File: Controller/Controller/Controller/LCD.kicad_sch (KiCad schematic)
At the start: 46 parts, among them IC1 LTC1261L, J8 Conn_01x06_MountingPin, J9 Conn_01x50_MountingPin, Q1 CSD16323Q3, U4 LM317L_SO8, U5 AMS1117-3.3, U6 LM317L_SO8, U7 LM3488, U8 C85037, U9 LM317L_SO8

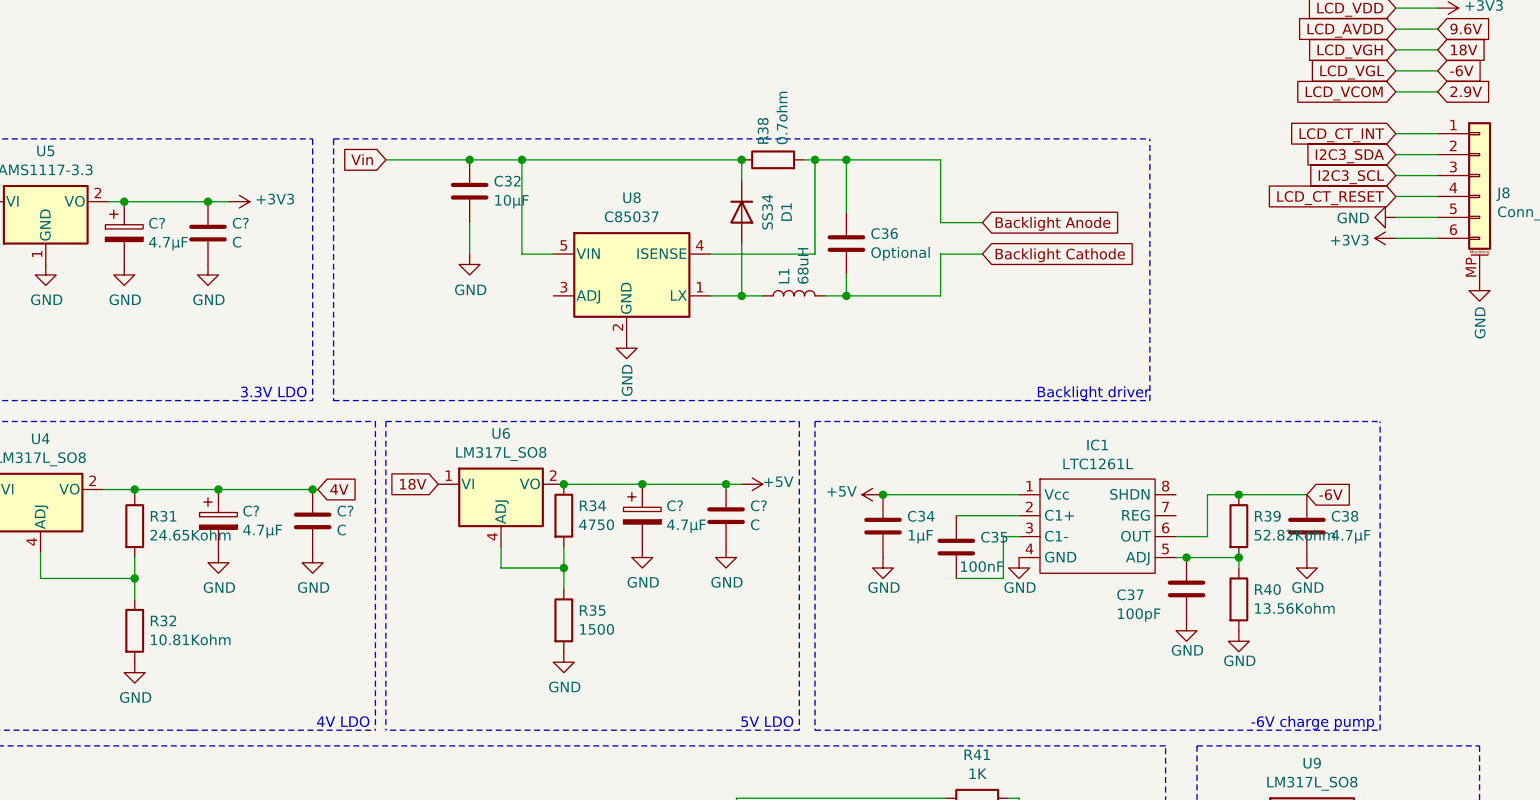
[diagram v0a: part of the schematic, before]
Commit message: changed LCDboard to Controller
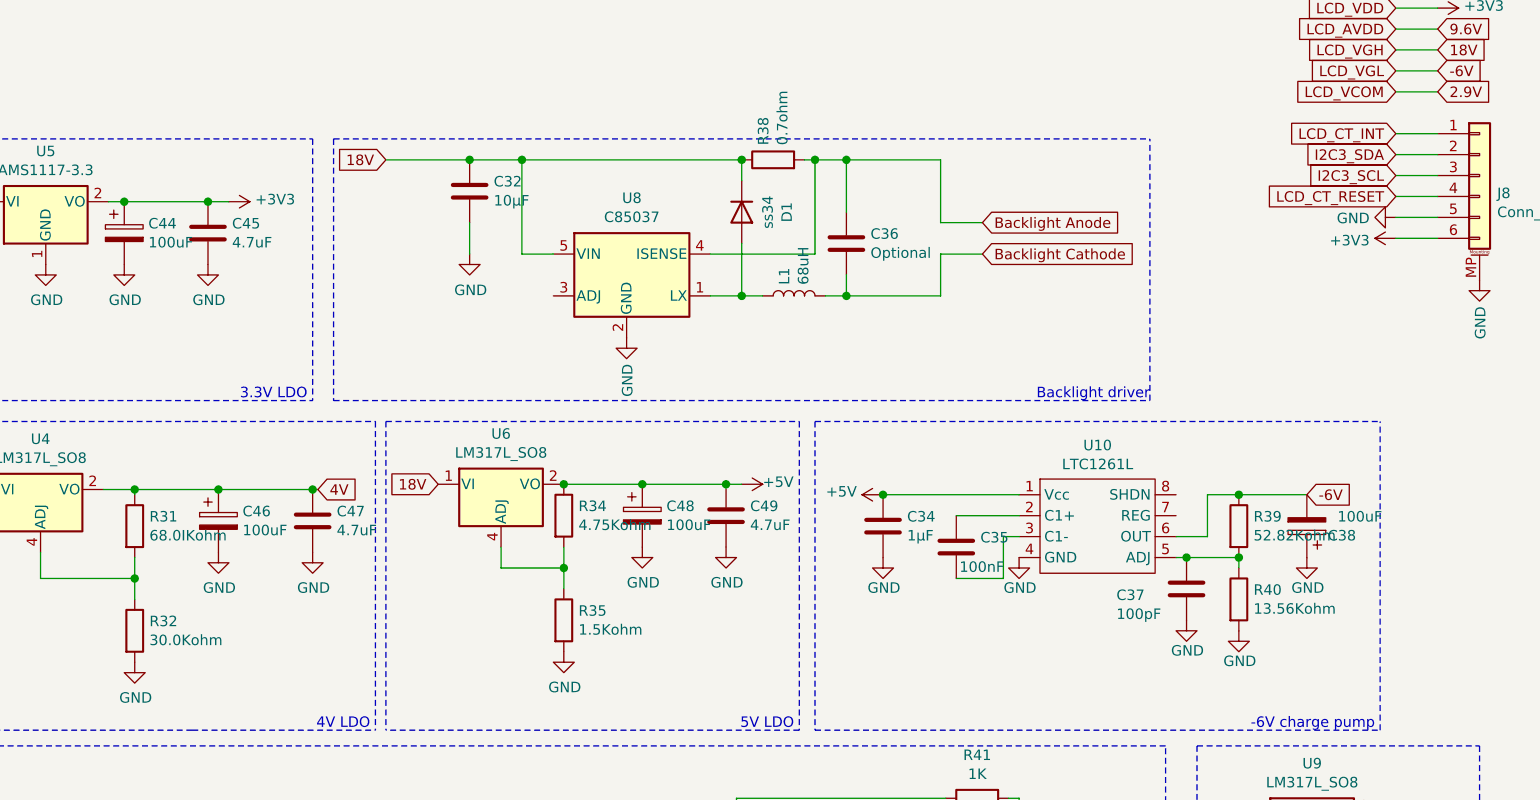
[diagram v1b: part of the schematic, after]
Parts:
- removed C38: 4.7µF, symbol Device:C
- added C38: 100uF, Capacitor_SMD:CP_Elec_5x5.4, symbol Device:CP
- C28: footprint (none) -> Capacitor_SMD:CP_Elec_8x10; LCSC (none) -> C249647
- C29, C35: footprint (none) -> Capacitor_SMD:C_0805_2012Metric_Pad1.18x1.45mm_HandSolder
- C30: footprint (none) -> Capacitor_SMD:C_0805_2012Metric_Pad1.18x1.45mm_HandSolder; LCSC (none) -> C1829
- C31: footprint (none) -> Capacitor_SMD:C_0805_2012Metric_Pad1.18x1.45mm_HandSolder; LCSC (none) -> C282778
- C32: footprint Capacitor_SMD:C_1206_3216Metric_Pad1.42x1.75mm_HandSolder -> Capacitor_SMD:C_0805_2012Metric_Pad1.18x1.45mm_HandSolder; LCSC (none) -> C17024
- C33: footprint (none) -> Capacitor_SMD:C_0805_2012Metric_Pad1.18x1.45mm_HandSolder; LCSC (none) -> C157608
- C34: footprint (none) -> Capacitor_SMD:C_0805_2012Metric_Pad1.18x1.45mm_HandSolder; LCSC (none) -> C50683
- C36: footprint Capacitor_SMD:C_0805_2012Metric_Pad1.15x1.40mm_HandSolder -> Capacitor_SMD:C_1206_3216Metric_Pad1.33x1.80mm_HandSolder
- C37: footprint (none) -> Capacitor_SMD:C_0805_2012Metric_Pad1.18x1.45mm_HandSolder; LCSC (none) -> C82028
- C39: footprint (none) -> Capacitor_SMD:CP_Elec_10x12.6; LCSC (none) -> C250070
- C44, C46, C48: renamed from C?; value 4.7µF -> 100uF; footprint (none) -> Capacitor_SMD:CP_Elec_5x5.4
- C45, C47, C49: renamed from C?; value C -> 4.7uF; footprint (none) -> Capacitor_SMD:C_0805_2012Metric_Pad1.18x1.45mm_HandSolder; LCSC (none) -> C415307
- D1: value SS34 -> ss34; LCSC (none) -> C83961
- D2: footprint (none) -> Diode_SMD:D_SMA_Handsoldering; LCSC (none) -> C83961
- J8: footprint (none) -> Connector_FFC-FPC:Hirose_FH12-6S-0.5SH_1x06-1MP_P0.50mm_Horizontal; LCSC (none) -> C528032
- J9: footprint (none) -> 00_Custom_Kicad:FPC_50; LCSC (none) -> C11098
- L2: footprint (none) -> Inductor_SMD:L_6.3x6.3_H3; LCSC (none) -> C326333
- R31: value 24.65Kohm -> 68.0IKohm; footprint (none) -> Resistor_SMD:R_0805_2012Metric_Pad1.20x1.40mm_HandSolder; LCSC (none) -> C294735
- R32: value 10.81Kohm -> 30.0Kohm; footprint (none) -> Resistor_SMD:R_0805_2012Metric_Pad1.20x1.40mm_HandSolder; LCSC (none) -> C40087
- R34: value 4750 -> 4.75Kohm; footprint (none) -> Resistor_SMD:R_0805_2012Metric_Pad1.20x1.40mm_HandSolder; LCSC (none) -> C706245
- R35: value 1500 -> 1.5Kohm; footprint (none) -> Resistor_SMD:R_0805_2012Metric_Pad1.20x1.40mm_HandSolder; LCSC (none) -> C203762
- R36: footprint (none) -> Resistor_SMD:R_0805_2012Metric_Pad1.20x1.40mm_HandSolder
- U10: renamed from IC1; footprint (none) -> Package_SO:MSOP-8_3x3mm_P0.65mm
- U7: footprint (none) -> Package_SO:MSOP-8_3x3mm_P0.65mm; LCSC (none) -> C80773
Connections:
- net -6V: now also C38.2
- net 18V: now also C32.1, D1.1 (K), R38.1, U8.5 (VIN)
- net GND: now also C38.1
- net Vin: no longer C32.1, D1.1 (K), R38.1, U8.5 (VIN)

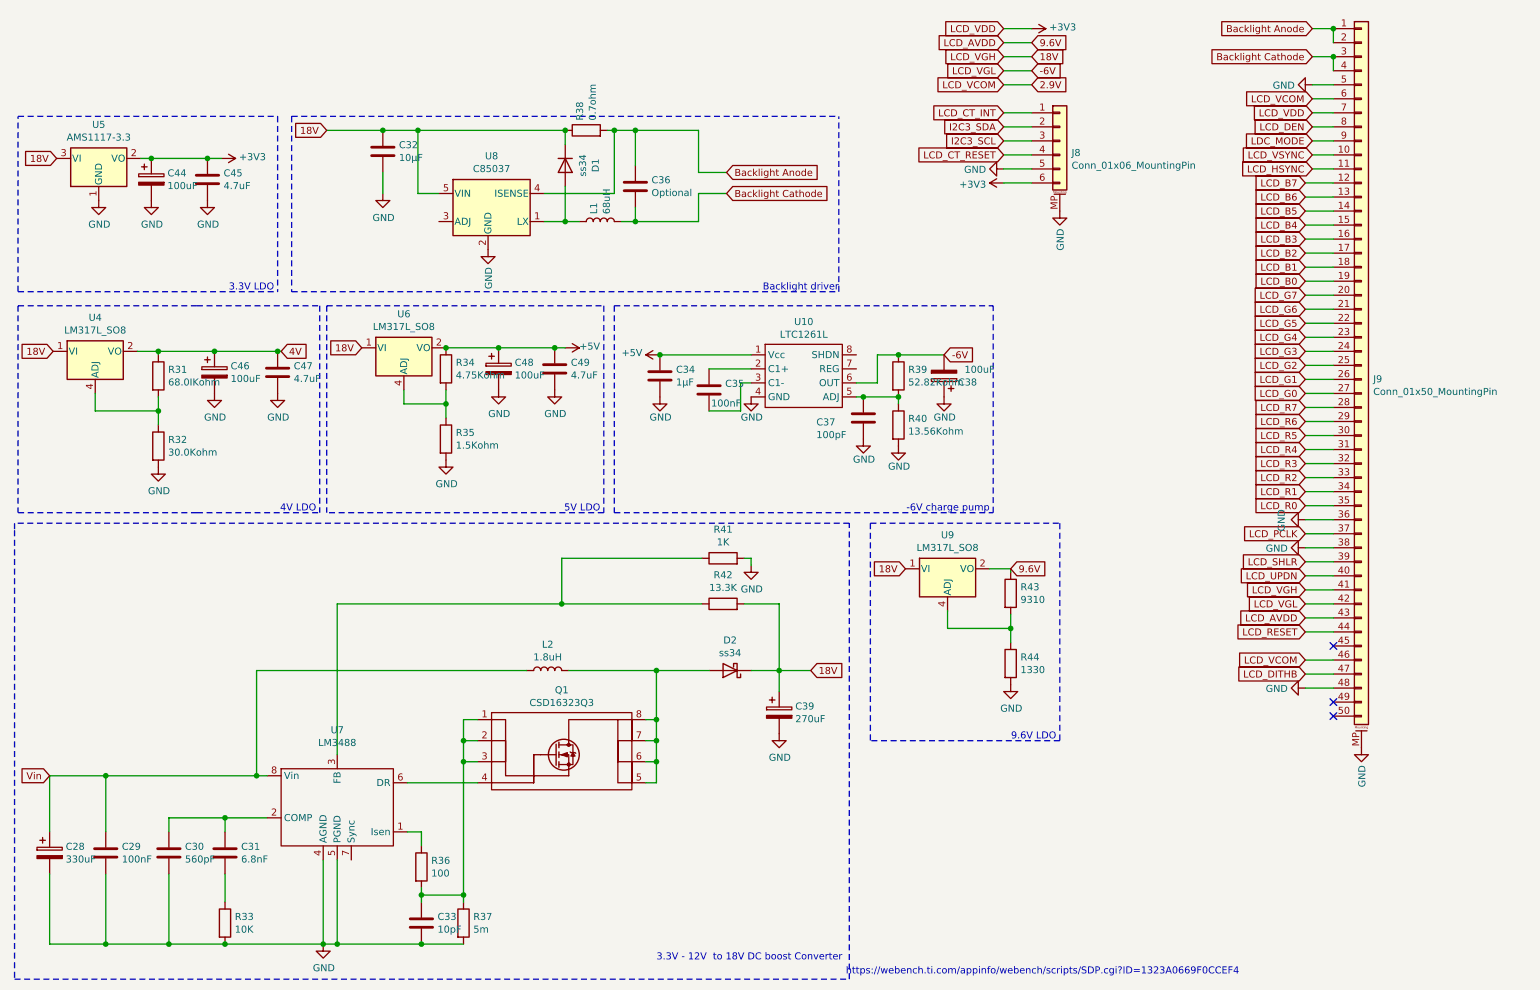
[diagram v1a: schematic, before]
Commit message: Rev 1 LCD contoller board
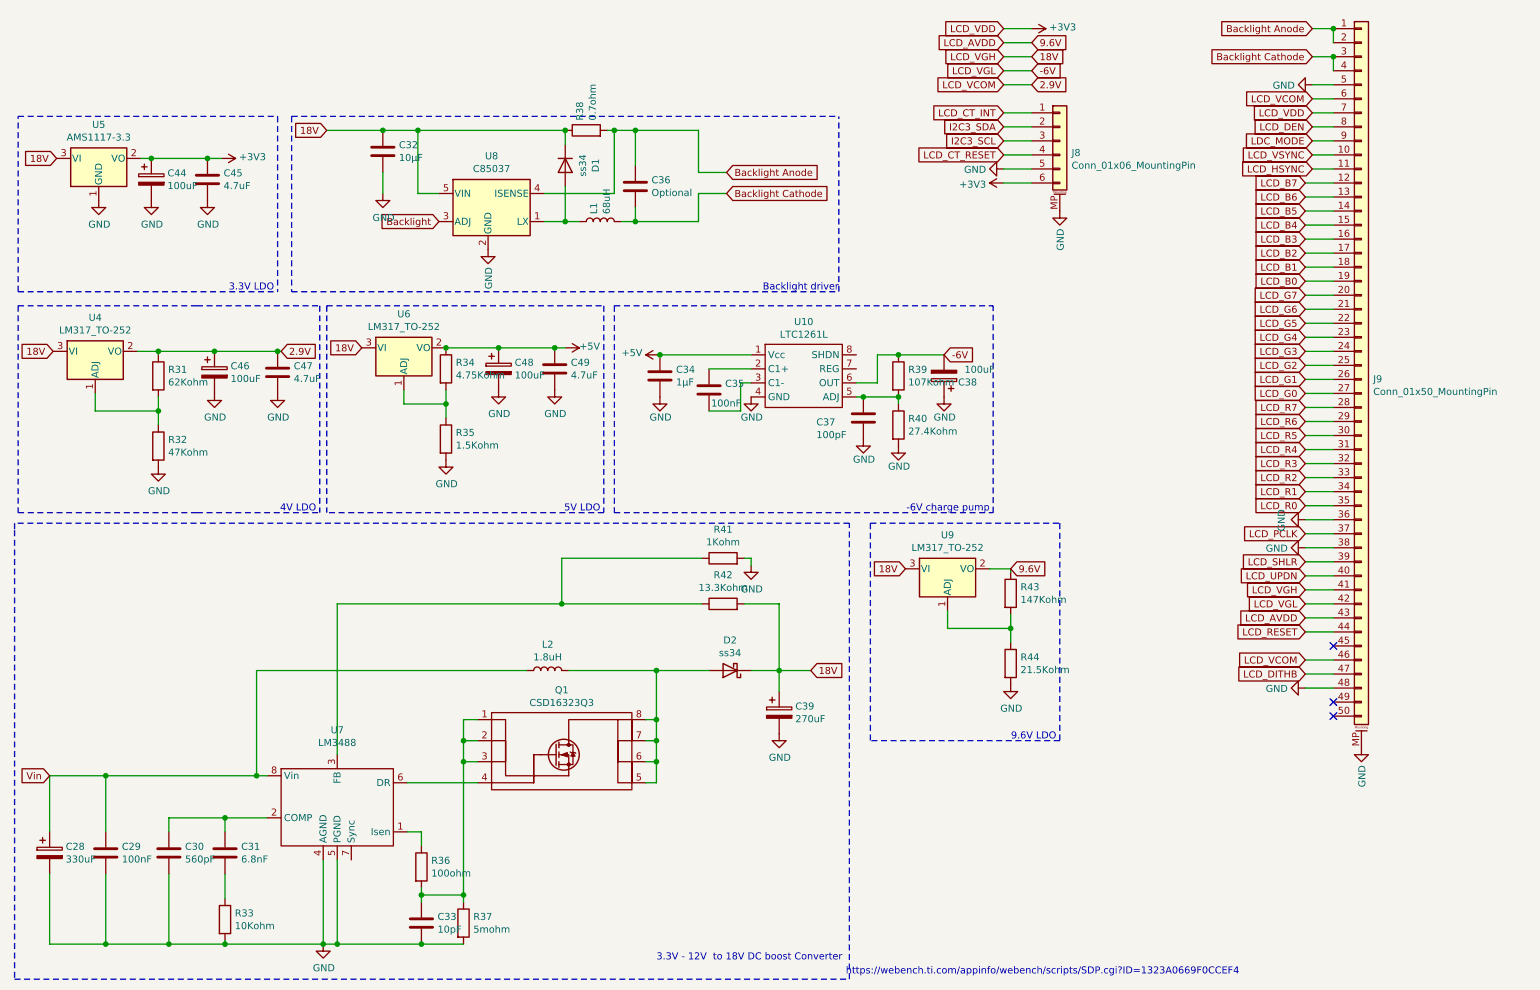
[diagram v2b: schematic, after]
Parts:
- removed U4, U6, U9: LM317L_SO8, Package_SO:SOIC-8_3.9x4.9mm_P1.27mm, symbol Regulator_Linear:LM317L_SO8
- added U4, U6, U9: LM317_TO-252, Package_TO_SOT_SMD:TO-252-2, symbol Regulator_Linear:LM317_TO-252
- C32: footprint Capacitor_SMD:C_0805_2012Metric_Pad1.18x1.45mm_HandSolder -> Capacitor_SMD:C_1206_3216Metric_Pad1.33x1.80mm_HandSolder
- R31: value 68.0IKohm -> 62Kohm; LCSC C294735 -> C351556
- R32: value 30.0Kohm -> 47Kohm; LCSC C40087 -> (none)
- R33: value 10K -> 10Kohm; footprint (none) -> Resistor_SMD:R_0805_2012Metric_Pad1.20x1.40mm_HandSolder
- R36: value 100 -> 100ohm
- R37: value 5m -> 5mohm; footprint (none) -> Resistor_SMD:R_2512_6332Metric_Pad1.40x3.35mm_HandSolder; LCSC (none) -> C782251
- R38: footprint Resistor_SMD:R_1206_3216Metric_Pad1.42x1.75mm_HandSolder -> Resistor_SMD:R_1206_3216Metric_Pad1.30x1.75mm_HandSolder; LCSC (none) -> C621283
- R39: value 52.82Kohm -> 107Kohm; footprint (none) -> Resistor_SMD:R_0805_2012Metric_Pad1.20x1.40mm_HandSolder; LCSC (none) -> C409944
- R40: value 13.56Kohm -> 27.4Kohm; footprint (none) -> Resistor_SMD:R_0805_2012Metric_Pad1.20x1.40mm_HandSolder; LCSC (none) -> C17587
- R41: value 1K -> 1Kohm; footprint (none) -> Resistor_SMD:R_0805_2012Metric_Pad1.20x1.40mm_HandSolder
- R42: value 13.3K -> 13.3Kohm; footprint (none) -> Resistor_SMD:R_0805_2012Metric_Pad1.20x1.40mm_HandSolder; LCSC (none) -> C103975
- R43: value 9310 -> 147Kohm; footprint (none) -> Resistor_SMD:R_0805_2012Metric_Pad1.20x1.40mm_HandSolder; LCSC (none) -> C170031
- R44: value 1330 -> 21.5Kohm; footprint (none) -> Resistor_SMD:R_0805_2012Metric_Pad1.20x1.40mm_HandSolder; LCSC (none) -> C706267
- U5: LCSC (none) -> C347222
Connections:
- net 4V is gone; now on net 2.9V: C46.1, C47.1, R31.1
- net +5V: now also U6.2 (VO)
- net 18V: now also U4.3 (VI), U6.3 (VI), U9.3 (VI)
- net 2.9V: now also U4.2 (VO)
- net 9.6V: now also U9.2 (VO)
- net at R31.2, R32.1: now also U4.1 (ADJ)
- net at R34.2, R35.1: now also U6.1 (ADJ)
- net at R43.2, R44.1: now also U9.1 (ADJ)
- net Backlight: now reaches U8.3 (ADJ)
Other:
- moved on the sheet: R33

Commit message: contoller and contoller front Rev 1
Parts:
- added C50: 100uF, Capacitor_SMD:CP_Elec_5x5.4, symbol Device:CP
- added C51: 4.7uF, Capacitor_SMD:C_0805_2012Metric_Pad1.18x1.45mm_HandSolder, symbol Device:C
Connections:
- net 9.6V: now also C50.1, C51.1
- net GND: now also C50.2, C51.2
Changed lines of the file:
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@@
   (junction (at 179.07 79.375) (diameter 1.016) (color 0 0 0 0))
   (junction (at 179.07 86.995) (diameter 1.016) (color 0 0 0 0))
+  (junction (at 199.39 118.11) (diameter 1.016) (color 0 0 0 0))
   (junction (at 199.39 128.905) (diameter 1.016) (color 0 0 0 0))
+  (junction (at 208.915 118.11) (diameter 1.016) (color 0 0 0 0))
+  (junction (at 219.075 118.11) (diameter 1.016) (color 0 0 0 0))
   (junction (at 257.81 20.32) (diameter 1.016) (color 0 0 0 0))
   (junction (at 257.81 25.4) (diameter 1.016) (color 0 0 0 0))
@@
     (stroke (width 0) (type solid) (color 0 0 0 0))
   )
+  (wire (pts (xy 199.39 118.11) (xy 208.915 118.11))
+    (stroke (width 0) (type solid) (color 0 0 0 0))
+  )
   (wire (pts (xy 199.39 118.745) (xy 199.39 118.11))
     (stroke (width 0) (type solid) (color 0 0 0 0))
@@
     (stroke (width 0) (type solid) (color 0 0 0 0))
   )
+  (wire (pts (xy 208.915 118.11) (xy 219.075 118.11))
+    (stroke (width 0) (type solid) (color 0 0 0 0))
+  )
+  (wire (pts (xy 219.075 118.11) (xy 220.345 118.11))
+    (stroke (width 0) (type solid) (color 0 0 0 0))
+  )
   (wire (pts (xy 252.73 48.26) (xy 257.81 48.26))
     (stroke (width 0) (type solid) (color 0 0 0 0))
@@
     (stroke (width 0) (type dash) (color 0 0 0 0))
   )
-  (polyline (pts (xy 173.99 109.855) (xy 208.28 109.855))
+  (polyline (pts (xy 173.99 109.855) (xy 228.6 109.855))
     (stroke (width 0) (type dash) (color 0 0 0 0))
   )
@@
     (stroke (width 0) (type dash) (color 0 0 0 0))
   )
-  (polyline (pts (xy 208.28 109.855) (xy 208.28 149.225))
-    (stroke (width 0) (type dash) (color 0 0 0 0))
-  )
-  (polyline (pts (xy 208.28 149.225) (xy 173.99 149.225))
+  (polyline (pts (xy 228.6 109.855) (xy 228.6 149.225))
+    (stroke (width 0) (type dash) (color 0 0 0 0))
+  )
+  (polyline (pts (xy 228.6 149.225) (xy 173.99 149.225))
     (stroke (width 0) (type dash) (color 0 0 0 0))
   )
@@
     (effects (font (size 1.27 1.27)) (justify right bottom))
   )
-  (text "9.6V LDO\n" (at 207.645 149.225 180)
+  (text "9.6V LDO\n" (at 227.965 149.225 180)
     (effects (font (size 1.27 1.27)) (justify right bottom))
   )
@@
     )
   )
-  (global_label "9.6V" (shape input) (at 199.39 118.11 0)
-    (effects (font (size 1.27 1.27)) (justify left))
-    (property "Intersheet References" "${INTERSHEET_REFS}" (id 0) (at 207.4395 118.0306 0)
-      (effects (font (size 1.27 1.27)) (justify left) hide)
-    )
-  )
   (global_label "9.6V" (shape input) (at 203.2 22.86 0)
     (effects (font (size 1.27 1.27)) (justify left))
@@
     )
   )
+  (global_label "9.6V" (shape input) (at 220.345 118.11 0)
+    (effects (font (size 1.27 1.27)) (justify left))
+    (property "Intersheet References" "${INTERSHEET_REFS}" (id 0) (at 228.3945 118.0306 0)
+      (effects (font (size 1.27 1.27)) (justify left) hide)
+    )
+  )
   (global_label "LCD_B7" (shape input) (at 252.73 48.26 180)
     (effects (font (size 1.27 1.27)) (justify right))
@@
     (pin "1")
   )
+  (symbol (lib_id "power:GND") (at 208.915 125.73 0) (unit 1)
+    (in_bom yes) (on_board yes)
+    (property "Reference" "#PWR0143" (id 0) (at 208.915 132.08 0)
+      (effects (font (size 1.27 1.27)) hide)
+    )
+    (property "Value" "GND" (id 1) (at 209.0293 130.0544 0))
+    (property "Footprint" "" (id 2) (at 208.915 125.73 0)
+      (effects (font (size 1.27 1.27)) hide)
+    )
+    (property "Datasheet" "" (id 3) (at 208.915 125.73 0)
+      (effects (font (size 1.27 1.27)) hide)
+    )
+    (pin "1")
+  )
+  (symbol (lib_id "power:GND") (at 219.075 125.73 0) (unit 1)
+    (in_bom yes) (on_board yes)
+    (property "Reference" "#PWR0142" (id 0) (at 219.075 132.08 0)
+      (effects (font (size 1.27 1.27)) hide)
+    )
+    (property "Value" "GND" (id 1) (at 219.1893 130.0544 0))
+    (property "Footprint" "" (id 2) (at 219.075 125.73 0)
+      (effects (font (size 1.27 1.27)) hide)
+    )
+    (property "Datasheet" "" (id 3) (at 219.075 125.73 0)
+      (effects (font (size 1.27 1.27)) hide)
+    )
+    (pin "1")
+  )
   (symbol (lib_id "power:GND") (at 252.73 109.22 270) (unit 1)
     (in_bom yes) (on_board yes)
@@
       (effects (font (size 1.27 1.27)) hide)
     )
+    (pin "1")
+    (pin "2")
+  )
+  (symbol (lib_id "Device:CP") (at 208.915 121.92 0) (unit 1)
+    (in_bom yes) (on_board yes)
+    (property "Reference" "C50" (id 0) (at 211.8361 120.7706 0)
+      (effects (font (size 1.27 1.27)) (justify left))
+    )
+    (property "Value" "100uF" (id 1) (at 211.836 123.069 0)
+      (effects (font (size 1.27 1.27)) (justify left))
+    )
+    (property "Footprint" "Capacitor_SMD:CP_Elec_5x5.4" (id 2) (at 209.8802 125.73 0)
+      (effects (font (size 1.27 1.27)) hide)
+    )
+    (property "Datasheet" "~" (id 3) (at 208.915 121.92 0)
+      (effects (font (size 1.27 1.27)) hide)
+    )
+    (pin "1")
+    (pin "2")
+  )
+  (symbol (lib_id "Device:C") (at 219.075 121.92 0) (unit 1)
+    (in_bom yes) (on_board yes)
+    (property "Reference" "C51" (id 0) (at 221.9961 120.7706 0)
+      (effects (font (size 1.27 1.27)) (justify left))
+    )
+    (property "Value" "4.7uF" (id 1) (at 221.9961 123.0693 0)
+      (effects (font (size 1.27 1.27)) (justify left))
+    )
+    (property "Footprint" "Capacitor_SMD:C_0805_2012Metric_Pad1.18x1.45mm_HandSolder" (id 2) (at 220.0402 125.73 0)
+      (effects (font (size 1.27 1.27)) hide)
+    )
+    (property "Datasheet" "~" (id 3) (at 219.075 121.92 0)
+      (effects (font (size 1.27 1.27)) hide)
+    )
+    (property "LCSC" "C415307" (id 4) (at 219.075 121.92 0)
+      (effects (font (size 1.27 1.27)) hide)
+    )
